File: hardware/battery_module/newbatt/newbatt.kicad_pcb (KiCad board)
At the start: 2 copper layers, 139 x 45 mm, 29 parts, among them J1 DC050-T, J2 Conn_01x10, U1 BQ24210DQCR

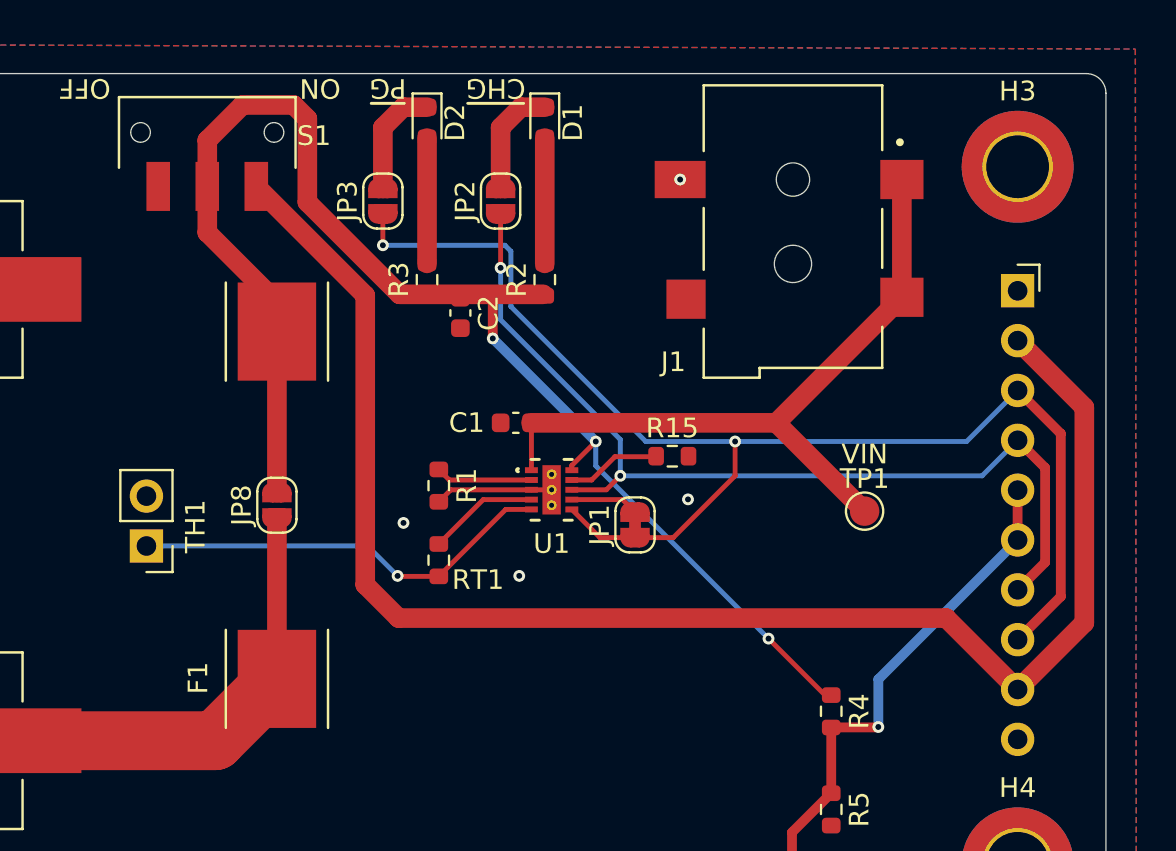
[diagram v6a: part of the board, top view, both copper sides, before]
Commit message: Added 3.3V linear regulator
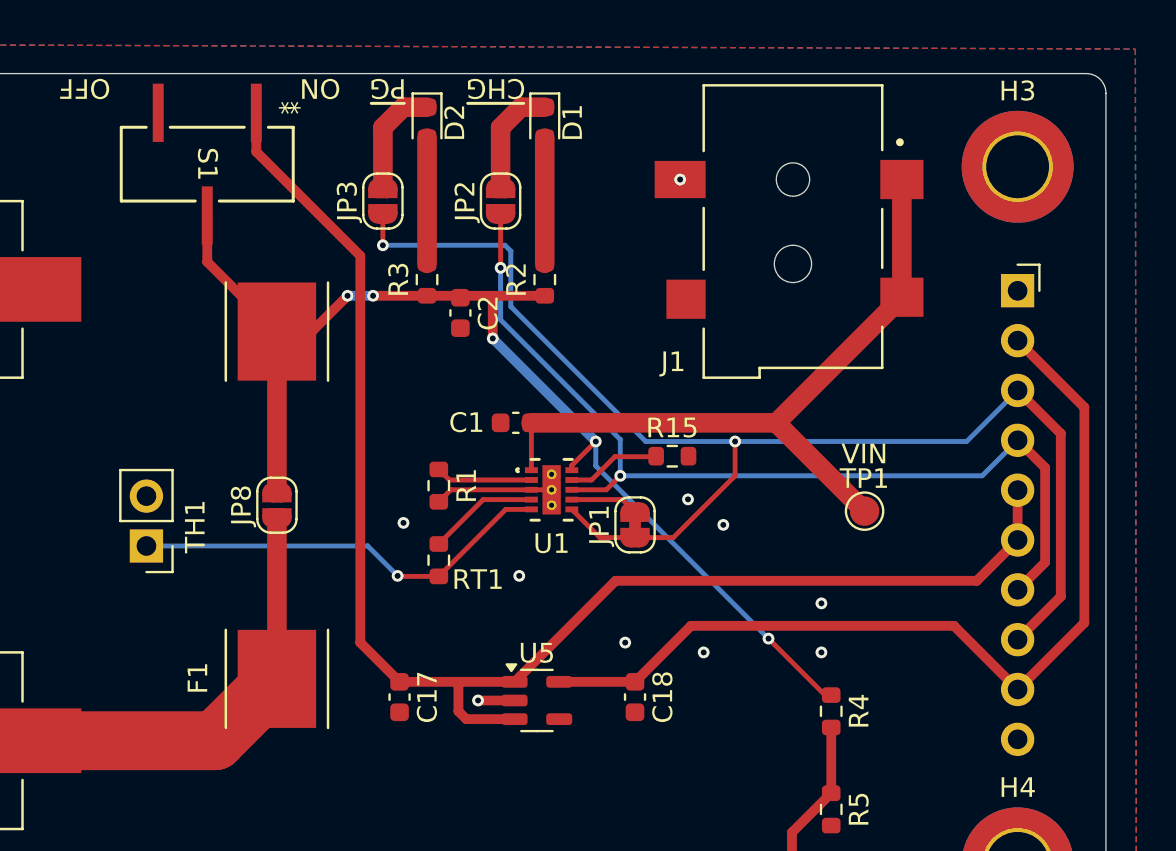
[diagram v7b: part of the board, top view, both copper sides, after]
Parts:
- added C17: 1 uF, Capacitor_SMD:C_0603_1608Metric, F.Cu at (118.0, 46.8)
- added C18: 1 uF, Capacitor_SMD:C_0603_1608Metric, F.Cu at (130.0, 46.8)
- added U5: XC6210B332MR, Package_TO_SOT_SMD:SOT-23-5, F.Cu at (125.0, 47.0)
- R15: value 500 Ohm -> 7.32 kOhm
- RT1: value R_Small_US -> 21.5 kOhm
- S1: value JS102011SAQN -> JS102011SCQN; footprint JS102011SAQN:SW_JS102011SAQN -> JS102011SCQN:SWITCH_1SCQN
- moved S1 1.62 mm to (108.2, 19.6), turned to -90 degrees
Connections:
- J2 pad 5: /VBAT/2 -> Net-(J2-Pin_5)
- J2 pad 6: /VBAT/2 -> Net-(J2-Pin_5)
- S1 pad 1: Net-(J2-Pin_2) -> Net-(J2-Pin_5)
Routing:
- net Net-(J2-Pin_5): track 0.00 -> 73.6 mm
- net Net-(J2-Pin_2): track 78.8 -> 46.6 mm
- net /VBAT/2: track 28.5 -> 11.1 mm, vias 1 -> 0
- net Net-(JP8-B): track 73.3 -> 59.6 mm, vias 3 -> 5
- net 0: track 6.00 -> 7.87 mm, vias 4 -> 10
